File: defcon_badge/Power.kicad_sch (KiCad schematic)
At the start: 15 parts, among them J10 USB_C_Receptacle_USB2.0_16P, J11 JST-PH 2P, SW1 SS-12D00, U10 TP4056, U11 ME6211C33M5G

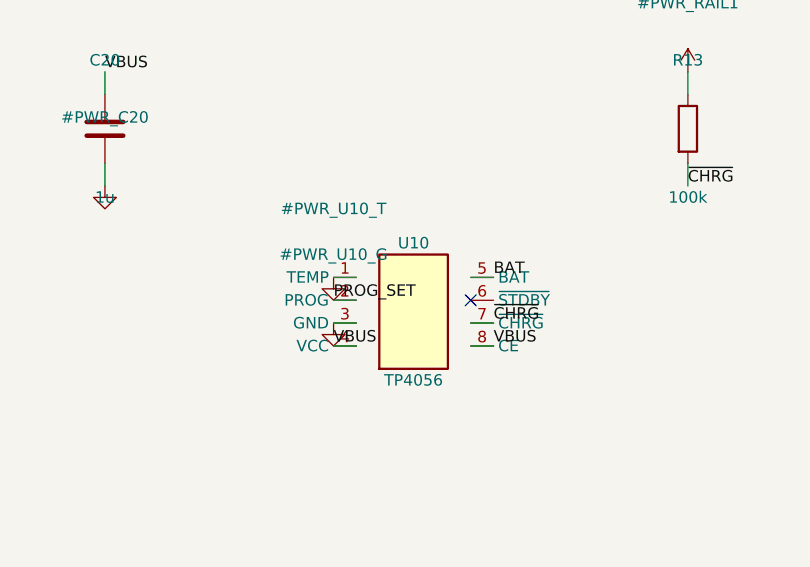
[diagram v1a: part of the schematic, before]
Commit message: Schematic: TP4056 ESOP-8 exposed pad + fix generator odd-pin-count layout
- TP4056 (U10): add pin 9 (EP, exposed thermal pad) tied to GND and switch to the
  stock ESOP-8 footprint (HSOP-8-1EP ...ThermalVias). The TP4056 is ESOP-8 and the
  EP must be soldered to GND for its rated 1A charge dissipation — this was missing
  and is invisible to ERC (no EP pin to flag).
- kicad_sheet_gen.py: fix a pin-layout bug surfaced by the 9-pin symbol. When the two
  sides have unequal pin counts (5 left / 4 right), pin_y distributed the shorter side
  over the taller body to off-grid Y, so label stubs snapped off pins 6/7 (spurious
  opens). Snap pin Y to the 1.27mm grid; no-op for the existing equal-side symbols.

Verified: U10.9(EP)->GND, U10.7->~CHRG, DAC/LED chains unchanged, ERC 0 errors.
(MCU_Core has no generator — it's patch-script maintained — so RUN pull-up and the
ADC filter will come via a patch script next.)

Co-Authored-By: Claude Opus 4.8 (1M context) <noreply@anthropic.com>
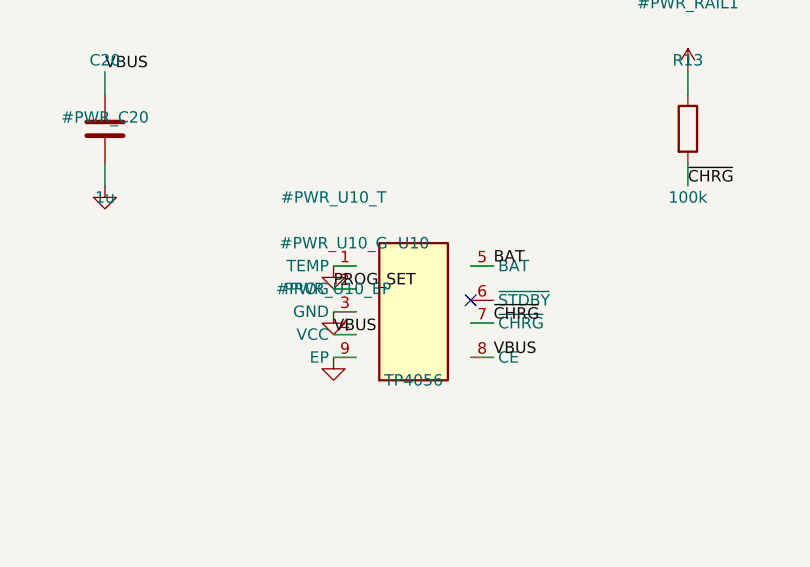
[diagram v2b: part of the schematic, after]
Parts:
- U10: footprint Package_SO:SOIC-8_3.9x4.9mm_P1.27mm -> Package_SO:HSOP-8-1EP_3.9x4.9mm_P1.27mm_EP2.3x2.3mm_ThermalVias
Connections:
- net GND: now also U10.9 (EP)
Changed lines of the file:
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@@
 		(property "Reference" "U10" (at 129.54 82.55 0) (effects (font (size 1.27 1.27))))
 		(property "Value" "TP4056" (at 129.54 97.79 0) (effects (font (size 1.27 1.27))))
-		(property "Footprint" "Package_SO:SOIC-8_3.9x4.9mm_P1.27mm" (at 129.54 90.17 0) (show_name no) (hide yes) (effects (font (size 1.27 1.27))))
+		(property "Footprint" "Package_SO:HSOP-8-1EP_3.9x4.9mm_P1.27mm_EP2.3x2.3mm_ThermalVias" (at 129.54 90.17 0) (show_name no) (hide yes) (effects (font (size 1.27 1.27))))
 		(property "Datasheet" "" (at 129.54 90.17 0) (show_name no) (hide yes) (effects (font (size 1.27 1.27))))
-		(property "Description" "Li-Ion 1A linear charger" (at 129.54 90.17 0) (show_name no) (hide yes) (effects (font (size 1.27 1.27))))
+		(property "Description" "Li-Ion 1A linear charger (ESOP-8)" (at 129.54 90.17 0) (show_name no) (hide yes) (effects (font (size 1.27 1.27))))
 		(property "MPN" "TP4056" (at 129.54 90.17 0) (show_name no) (hide yes) (effects (font (size 1.27 1.27))))
 		(property "LCSC" "C16581" (at 129.54 90.17 0) (show_name no) (hide yes) (effects (font (size 1.27 1.27))))
@@
 		(pin "3")
 		(pin "4")
+		(pin "9")
 		(pin "5")
 		(pin "6")
@@
 	(symbol
 		(lib_id "power:GND")
-		(at 120.65 86.36 0)
-		(unit 1)
-		(body_style 1)
-		(exclude_from_sim no)
-		(in_bom yes)
-		(on_board yes)
-		(in_pos_files yes)
-		(dnp no)
-		(fields_autoplaced yes)
-		(property "Reference" "#PWR_U10_T" (at 120.65 78.74 0) (effects (font (size 1.27 1.27))))
-		(property "Value" "GND" (at 120.65 93.98 0) (effects (font (size 1.27 1.27)) (hide yes)))
-		(property "Footprint" "" (at 120.65 86.36 0) (show_name no) (hide yes) (effects (font (size 1.27 1.27))))
-		(property "Datasheet" "" (at 120.65 86.36 0) (show_name no) (hide yes) (effects (font (size 1.27 1.27))))
-		(property "Description" "" (at 120.65 86.36 0) (show_name no) (hide yes) (effects (font (size 1.27 1.27))))
+		(at 120.65 85.09 0)
+		(unit 1)
+		(body_style 1)
+		(exclude_from_sim no)
+		(in_bom yes)
+		(on_board yes)
+		(in_pos_files yes)
+		(dnp no)
+		(fields_autoplaced yes)
+		(property "Reference" "#PWR_U10_T" (at 120.65 77.47 0) (effects (font (size 1.27 1.27))))
+		(property "Value" "GND" (at 120.65 92.71 0) (effects (font (size 1.27 1.27)) (hide yes)))
+		(property "Footprint" "" (at 120.65 85.09 0) (show_name no) (hide yes) (effects (font (size 1.27 1.27))))
+		(property "Datasheet" "" (at 120.65 85.09 0) (show_name no) (hide yes) (effects (font (size 1.27 1.27))))
+		(property "Description" "" (at 120.65 85.09 0) (show_name no) (hide yes) (effects (font (size 1.27 1.27))))
 		(pin "1")
 		(instances
@@
 	(symbol
 		(lib_id "power:GND")
-		(at 120.65 91.44 0)
-		(unit 1)
-		(body_style 1)
-		(exclude_from_sim no)
-		(in_bom yes)
-		(on_board yes)
-		(in_pos_files yes)
-		(dnp no)
-		(fields_autoplaced yes)
-		(property "Reference" "#PWR_U10_G" (at 120.65 83.82 0) (effects (font (size 1.27 1.27))))
-		(property "Value" "GND" (at 120.65 99.06 0) (effects (font (size 1.27 1.27)) (hide yes)))
-		(property "Footprint" "" (at 120.65 91.44 0) (show_name no) (hide yes) (effects (font (size 1.27 1.27))))
-		(property "Datasheet" "" (at 120.65 91.44 0) (show_name no) (hide yes) (effects (font (size 1.27 1.27))))
-		(property "Description" "" (at 120.65 91.44 0) (show_name no) (hide yes) (effects (font (size 1.27 1.27))))
+		(at 120.65 90.17 0)
+		(unit 1)
+		(body_style 1)
+		(exclude_from_sim no)
+		(in_bom yes)
+		(on_board yes)
+		(in_pos_files yes)
+		(dnp no)
+		(fields_autoplaced yes)
+		(property "Reference" "#PWR_U10_G" (at 120.65 82.55 0) (effects (font (size 1.27 1.27))))
+		(property "Value" "GND" (at 120.65 97.79 0) (effects (font (size 1.27 1.27)) (hide yes)))
+		(property "Footprint" "" (at 120.65 90.17 0) (show_name no) (hide yes) (effects (font (size 1.27 1.27))))
+		(property "Datasheet" "" (at 120.65 90.17 0) (show_name no) (hide yes) (effects (font (size 1.27 1.27))))
+		(property "Description" "" (at 120.65 90.17 0) (show_name no) (hide yes) (effects (font (size 1.27 1.27))))
 		(pin "1")
 		(instances
@@
 				(path "/8c0b3d8b-46d3-4173-ab1e-a61765f77d61/5744f316-b81d-4687-a6bb-e0b6cbd3f68c"
 					(reference "#PWR_U10_G")
+					(unit 1)
+				)
+			)
+		)
+	)
+	(symbol
+		(lib_id "power:GND")
+		(at 120.65 95.25 0)
+		(unit 1)
+		(body_style 1)
+		(exclude_from_sim no)
+		(in_bom yes)
+		(on_board yes)
+		(in_pos_files yes)
+		(dnp no)
+		(fields_autoplaced yes)
+		(property "Reference" "#PWR_U10_EP" (at 120.65 87.63 0) (effects (font (size 1.27 1.27))))
+		(property "Value" "GND" (at 120.65 102.87 0) (effects (font (size 1.27 1.27)) (hide yes)))
+		(property "Footprint" "" (at 120.65 95.25 0) (show_name no) (hide yes) (effects (font (size 1.27 1.27))))
+		(property "Datasheet" "" (at 120.65 95.25 0) (show_name no) (hide yes) (effects (font (size 1.27 1.27))))
+		(property "Description" "" (at 120.65 95.25 0) (show_name no) (hide yes) (effects (font (size 1.27 1.27))))
+		(pin "1")
+		(instances
+			(project "defcon_badge"
+				(path "/8c0b3d8b-46d3-4173-ab1e-a61765f77d61/5744f316-b81d-4687-a6bb-e0b6cbd3f68c"
+					(reference "#PWR_U10_EP")
 					(unit 1)
 				)
@@
 	(wire (pts (xy 95.25 66.04) (xy 95.25 63.50)) (stroke (width 0) (type default)))
 	(wire (pts (xy 95.25 73.66) (xy 95.25 76.20)) (stroke (width 0) (type default)))
-	(wire (pts (xy 123.19 86.36) (xy 120.65 86.36)) (stroke (width 0) (type default)))
-	(wire (pts (xy 123.19 88.90) (xy 120.65 88.90)) (stroke (width 0) (type default)))
-	(wire (pts (xy 123.19 91.44) (xy 120.65 91.44)) (stroke (width 0) (type default)))
-	(wire (pts (xy 123.19 93.98) (xy 120.65 93.98)) (stroke (width 0) (type default)))
-	(wire (pts (xy 135.89 86.36) (xy 138.43 86.36)) (stroke (width 0) (type default)))
+	(wire (pts (xy 123.19 85.09) (xy 120.65 85.09)) (stroke (width 0) (type default)))
+	(wire (pts (xy 123.19 87.63) (xy 120.65 87.63)) (stroke (width 0) (type default)))
+	(wire (pts (xy 123.19 90.17) (xy 120.65 90.17)) (stroke (width 0) (type default)))
+	(wire (pts (xy 123.19 92.71) (xy 120.65 92.71)) (stroke (width 0) (type default)))
+	(wire (pts (xy 135.89 85.09) (xy 138.43 85.09)) (stroke (width 0) (type default)))
 	(wire (pts (xy 135.89 91.44) (xy 138.43 91.44)) (stroke (width 0) (type default)))
-	(wire (pts (xy 135.89 93.98) (xy 138.43 93.98)) (stroke (width 0) (type default)))
+	(wire (pts (xy 135.89 95.25) (xy 138.43 95.25)) (stroke (width 0) (type default)))
+	(wire (pts (xy 123.19 95.25) (xy 120.65 95.25)) (stroke (width 0) (type default)))
 	(wire (pts (xy 115.57 125.73) (xy 115.57 123.19)) (stroke (width 0) (type default)))
 	(wire (pts (xy 115.57 133.35) (xy 115.57 135.89)) (stroke (width 0) (type default)))
@@
 	(label "CC2" (at 63.50 123.19 0) (effects (font (size 1.27 1.27)) (justify left bottom)))
 	(label "VBUS" (at 95.25 63.50 0) (effects (font (size 1.27 1.27)) (justify left bottom)))
-	(label "PROG_SET" (at 120.65 88.90 0) (effects (font (size 1.27 1.27)) (justify left bottom)))
-	(label "VBUS" (at 120.65 93.98 0) (effects (font (size 1.27 1.27)) (justify left bottom)))
-	(label "BAT" (at 138.43 86.36 0) (effects (font (size 1.27 1.27)) (justify left bottom)))
+	(label "PROG_SET" (at 120.65 87.63 0) (effects (font (size 1.27 1.27)) (justify left bottom)))
+	(label "VBUS" (at 120.65 92.71 0) (effects (font (size 1.27 1.27)) (justify left bottom)))
+	(label "BAT" (at 138.43 85.09 0) (effects (font (size 1.27 1.27)) (justify left bottom)))
 	(label "~{CHRG}" (at 138.43 91.44 0) (effects (font (size 1.27 1.27)) (justify left bottom)))
-	(label "VBUS" (at 138.43 93.98 0) (effects (font (size 1.27 1.27)) (justify left bottom)))
+	(label "VBUS" (at 138.43 95.25 0) (effects (font (size 1.27 1.27)) (justify left bottom)))
 	(label "PROG_SET" (at 115.57 123.19 0) (effects (font (size 1.27 1.27)) (justify left bottom)))
 	(label "~{CHRG}" (at 160.02 76.20 0) (effects (font (size 1.27 1.27)) (justify left bottom)))
